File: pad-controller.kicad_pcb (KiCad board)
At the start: 2 copper layers, 86 x 64 mm, 51 parts, among them J4 Conn_01x02, J6 Wago Terminal Block, M1 Motor_Servo, M2 Motor_Servo, M3 Motor_Servo, M4 Motor_Servo, Q2 FQP30N06L, SW1 SW_Push_Dual, U1 XBee, U2 TPS56121, U3 LD1117S33TR_SOT223

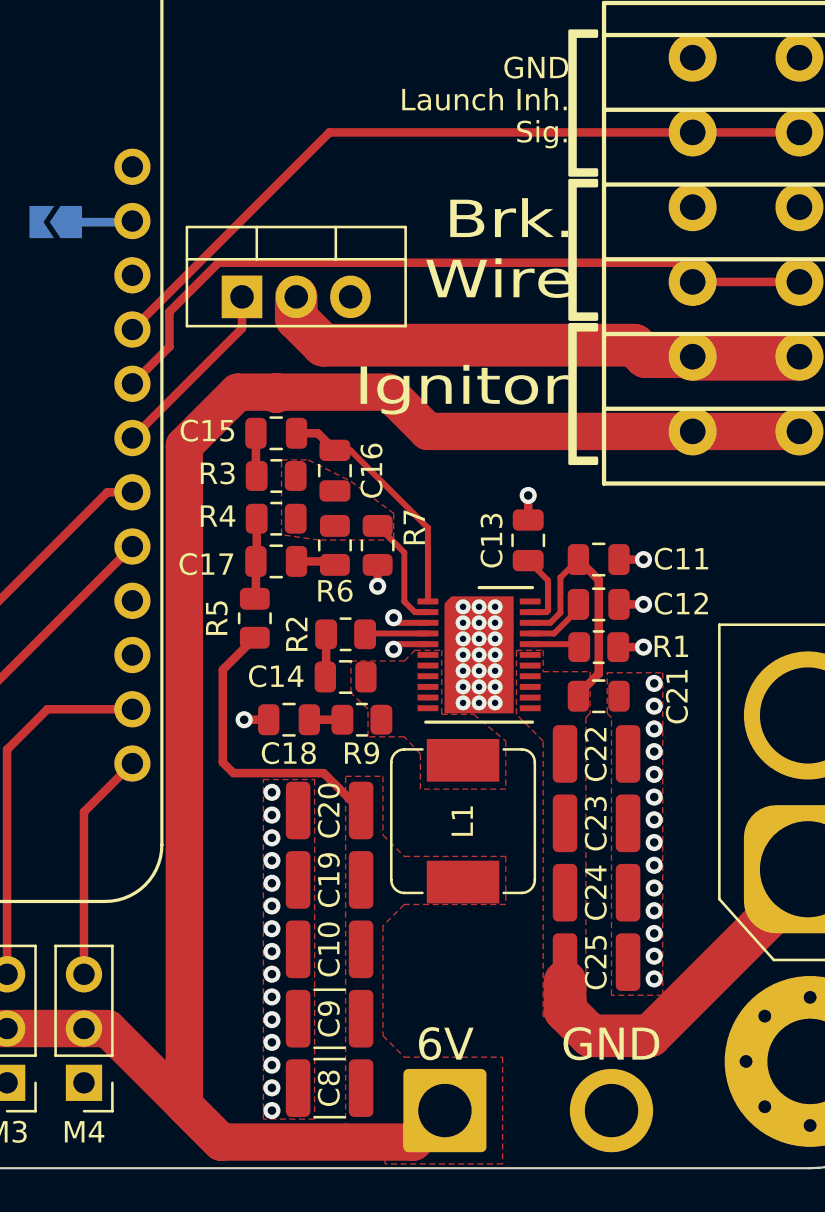
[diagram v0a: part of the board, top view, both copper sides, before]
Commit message: Reassign Feather pins to free up pin 13
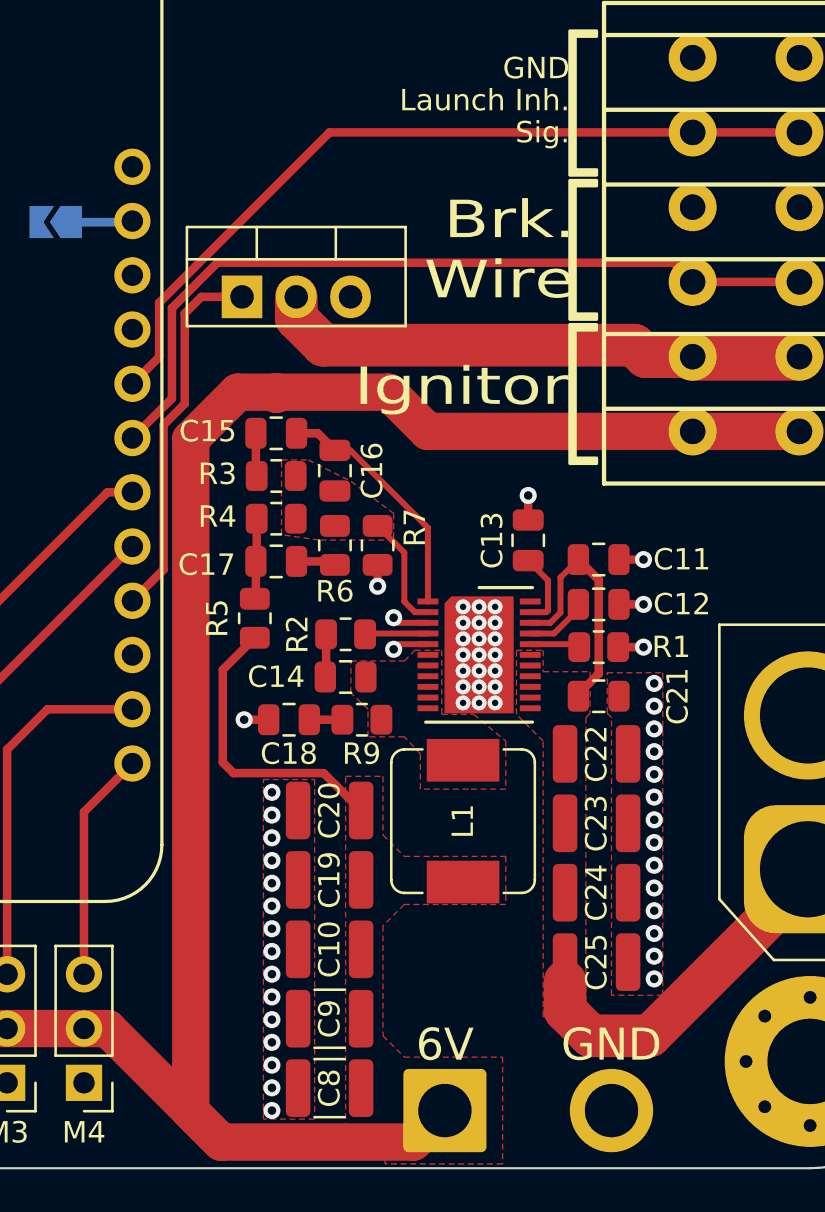
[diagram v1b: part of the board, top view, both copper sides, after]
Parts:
- R7: value 2.2777778 kΩ -> 2.26 kΩ
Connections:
- A1 pad 20: unconnected-(A1-D1-Pad20) -> E-Match
- A1 pad 23: E-Match -> Break Wire
- A1 pad 24: Break Wire -> Launch Inhibit
- A1 pad 25: Launch Inhibit -> unconnected-(A1-13-Pad25)
- U1 pad 16: XBee RTS -> unconnected-(U1-RTS/DIO6-Pad16)
- U1 pad 9: XBee DTR -> unconnected-(U1-DTR/SLEEP_RQ/DIO8-Pad9)
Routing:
- net E-Match: track 8.74 -> 17.5 mm
- net Break Wire: track 34.9 -> 37.5 mm
- net Launch Inhibit: track 35.1 -> 37.6 mm
